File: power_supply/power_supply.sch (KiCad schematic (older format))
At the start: 51 parts, among them J1 Conn_01x04_Male, J2 Conn_01x03_Male, J3 Conn_01x03_Male, J4 Conn_01x03_Male, J5 Conn_01x02_Male, J6 Conn_01x02_Male, U1 LM7815_TO220, U2 LM7915_TO220, U3 LM7815_TO220

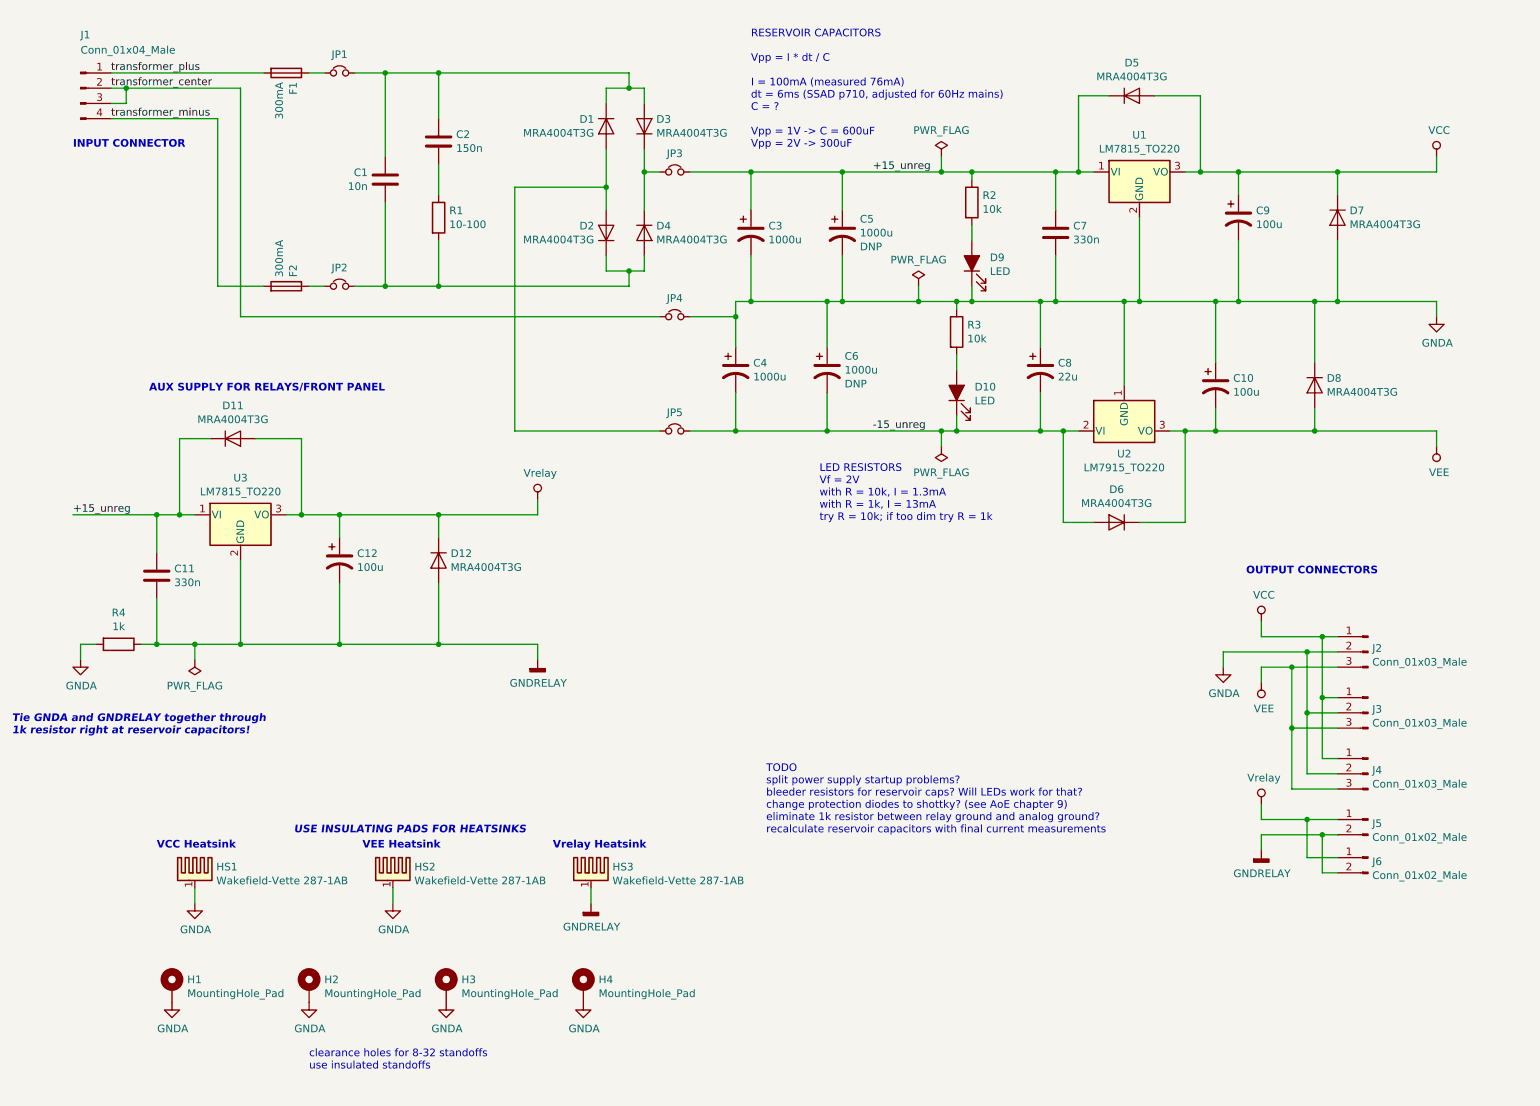
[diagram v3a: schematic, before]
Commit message: beautify schematic, update TODO, and tweak LEDs
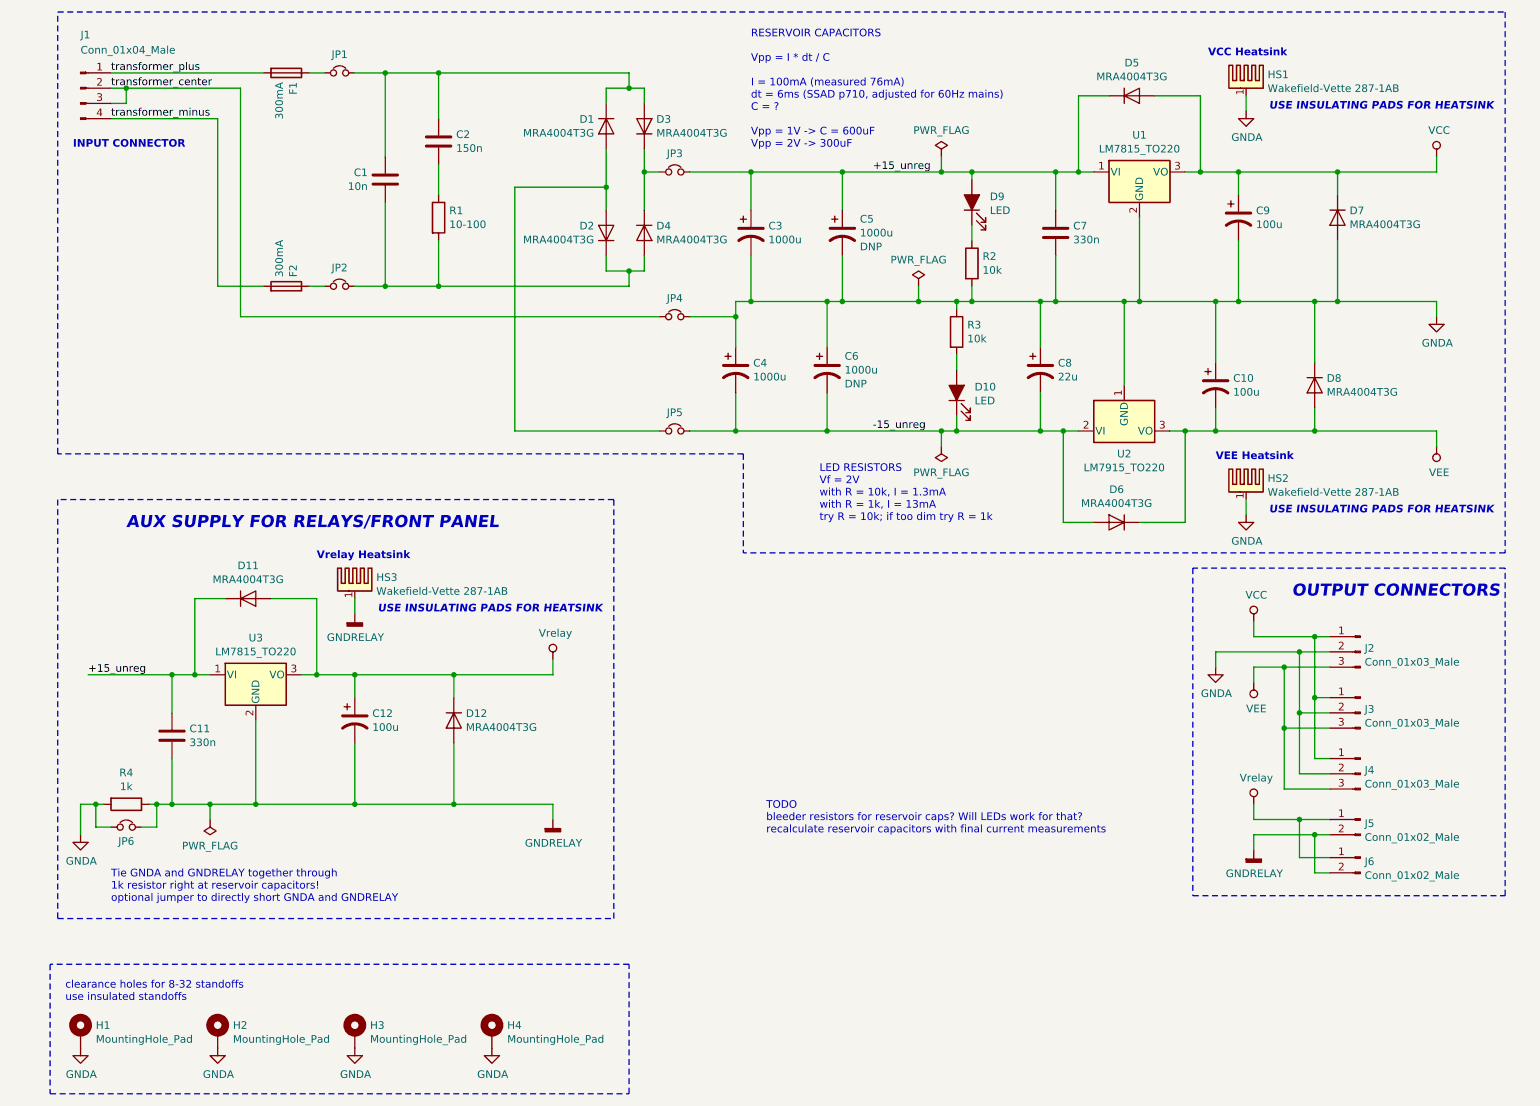
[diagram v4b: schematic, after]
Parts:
- added JP6: Jumper_NC_Small, Connector_PinHeader_2.54mm:PinHeader_1x02_P2.54mm_Vertical, symbol Device:Jumper_NC_Small
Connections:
- net +15_unreg: now also D9.2 (A); no longer R2.1
- net GNDA: now also R2.2, JP6.1; no longer D9.1 (K)
- net GNDRELAY: now also JP6.2
- new net: D9.1 (K), R2.1
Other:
- note added: "TODO\nbleeder resistors for reservoir caps? Will LEDs work for that?\nrecalculate reservoir capacitors with final current measurements"
- note added: "Tie GNDA and GNDRELAY together through\n1k resistor right at reservoir capacitors!\noptional jumper to directly short GNDA and GNDRELAY"
- note added: "USE INSULATING PADS FOR HEATSINK"
- note removed: "TODO\nsplit power supply startup problems?\nbleeder resistors for reservoir caps? Will LEDs work for that?\nchange protection diodes to shottky? (see AoE chapter 9)\neliminate 1k resistor between relay ground and analog ground?\nrecalculate reservoir capacitors with final current measurements"
- note removed: "Tie GNDA and GNDRELAY together through\n1k resistor right at reservoir capacitors!"
- note removed: "USE INSULATING PADS FOR HEATSINKS"
- moved on the sheet: C11, C12, D11, D12, D9, H1, H2, H3, H4, HS1, HS2, HS3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

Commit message: add OSHW/license to schematic
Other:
- note added: "CC-BY-SA 3.0"
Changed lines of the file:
@@
 	1    0    0    -1
 $EndComp
+$Comp
+L Graphic:Logo_Open_Hardware_Large #LOGO?
+U 1 1 5CFA7166
+P 5400 7400
+F 0 "#LOGO?" H 5400 7900 50  0001 C CNN
+F 1 "Logo_Open_Hardware_Large" H 5400 7000 50  0001 C CNN
+F 2 "" H 5400 7400 50  0001 C CNN
+F 3 "~" H 5400 7400 50  0001 C CNN
+	1    5400 7400
+	1    0    0    -1
+$EndComp
+Text Notes 5150 7900 0    50   ~ 10
+CC-BY-SA 3.0
 $EndSCHEMATC

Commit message: update text, and finalize damping resistor value
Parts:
- R1: value 10-100 -> 100
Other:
- note added: "RESERVOIR CAPACITORS\nC = I * dt / Vpp\n\nI = 250mA\ndt = 8.33ms\nVpp = 1-2V\n\nVpp = 1V -> C = 2000uF\nVpp = 2V -> C = 1000uF"
- note removed: "RESERVOIR CAPACITORS\n\nVpp = I * dt / C\n\nI = 100mA (measured 76mA)\ndt = 6ms (SSAD p710, adjusted for 60Hz mains)\nC = ?\n\nVpp = 1V -> C = 600uF\nVpp = 2V -> 300uF"
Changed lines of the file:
@@
 P 3350 2200
 F 0 "R1" H 3420 2246 50  0000 L CNN
-F 1 "10-100" H 3420 2155 50  0000 L CNN
+F 1 "100" H 3420 2155 50  0000 L CNN
 F 2 "Resistor_SMD:R_1206_3216Metric_Pad1.42x1.75mm_HandSolder" V 3280 2200 50  0001 C CNN
 F 3 "~" H 3350 2200 50  0001 C CNN
@@
 $EndComp
 Text Notes 5400 1750 0    50   ~ 0
-RESERVOIR CAPACITORS\n\nVpp = I * dt / C\n\nI = 100mA (measured 76mA)\ndt = 6ms (SSAD p710, adjusted for 60Hz mains)\nC = ?\n\nVpp = 1V -> C = 600uF\nVpp = 2V -> 300uF
+RESERVOIR CAPACITORS\nC = I * dt / Vpp\n\nI = 250mA\ndt = 8.33ms\nVpp = 1-2V\n\nVpp = 1V -> C = 2000uF\nVpp = 2V -> C = 1000uF
 Wire Wire Line
 	8250 4200 8250 3600

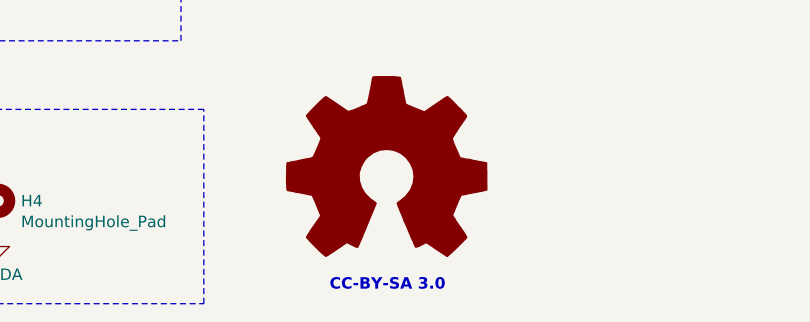
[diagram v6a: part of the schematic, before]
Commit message: change CC license version in schematic text from 3 to 4
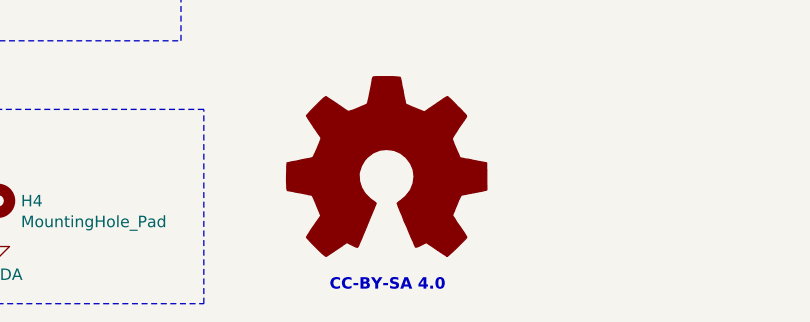
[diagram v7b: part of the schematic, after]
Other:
- note added: "CC-BY-SA 4.0"
- note removed: "CC-BY-SA 3.0"
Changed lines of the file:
@@
 	1    0    0    -1
 $EndComp
+Text Notes 5150 7900 0    50   ~ 10
+CC-BY-SA 4.0
 $Comp
-L Graphic:Logo_Open_Hardware_Large #LOGO?
+L Graphic:Logo_Open_Hardware_Large #LOGO1
 U 1 1 5CFA7166
 P 5400 7400
-F 0 "#LOGO?" H 5400 7900 50  0001 C CNN
+F 0 "#LOGO1" H 5400 7900 50  0001 C CNN
 F 1 "Logo_Open_Hardware_Large" H 5400 7000 50  0001 C CNN
 F 2 "" H 5400 7400 50  0001 C CNN
@@
 	1    0    0    -1
 $EndComp
-Text Notes 5150 7900 0    50   ~ 10
-CC-BY-SA 3.0
 $EndSCHEMATC

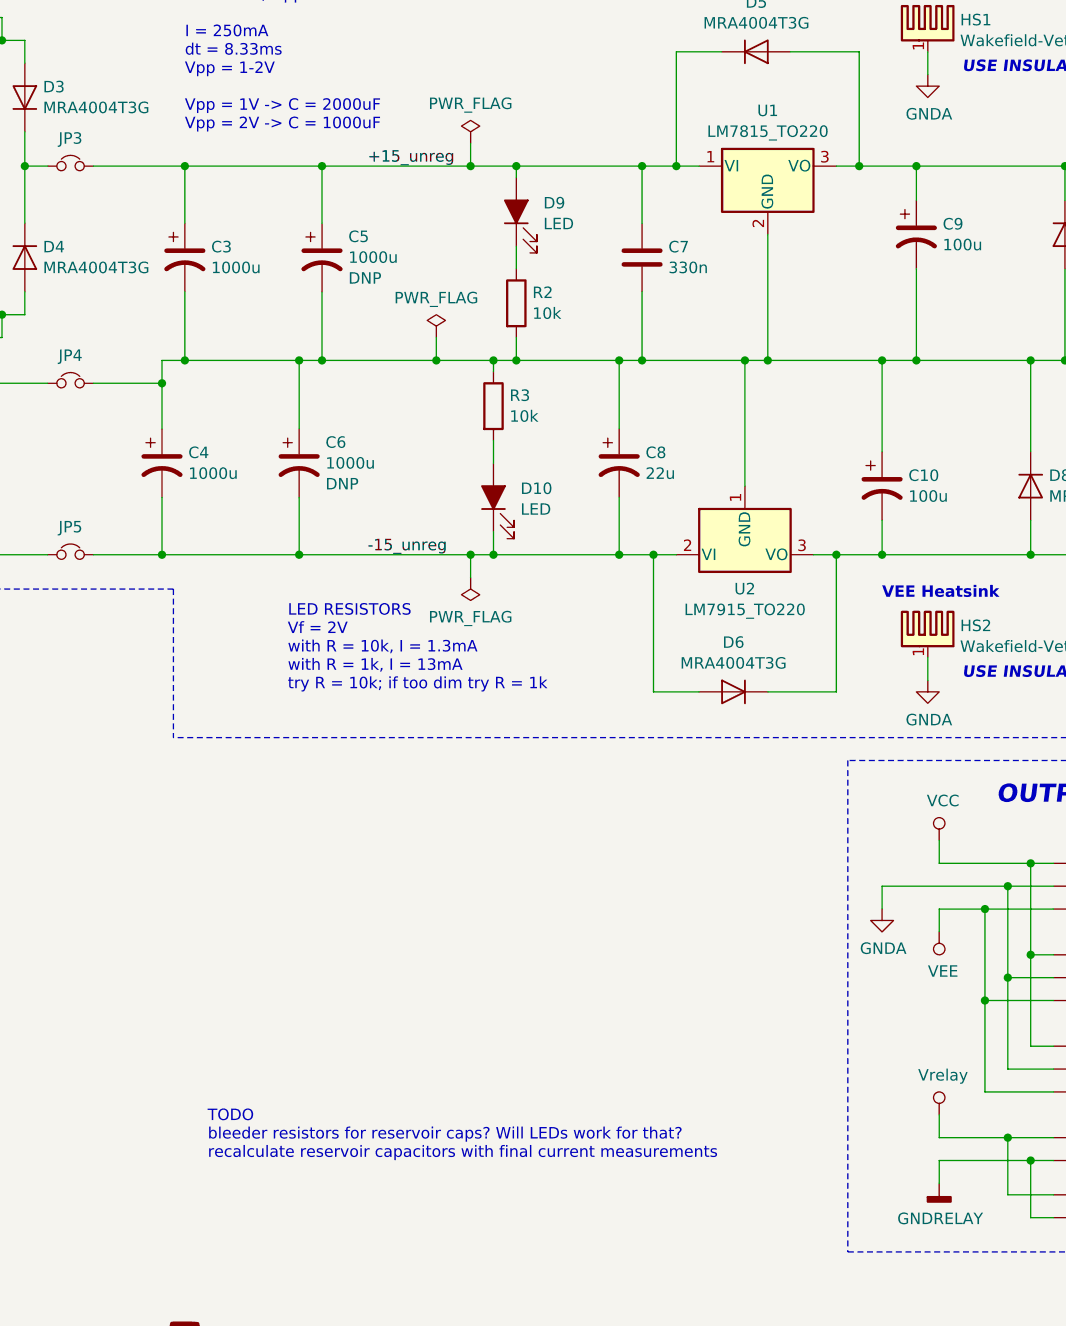
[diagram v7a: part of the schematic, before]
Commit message: remove second set of reservoir caps (deemed unnecessary for ripple and take up too much space)
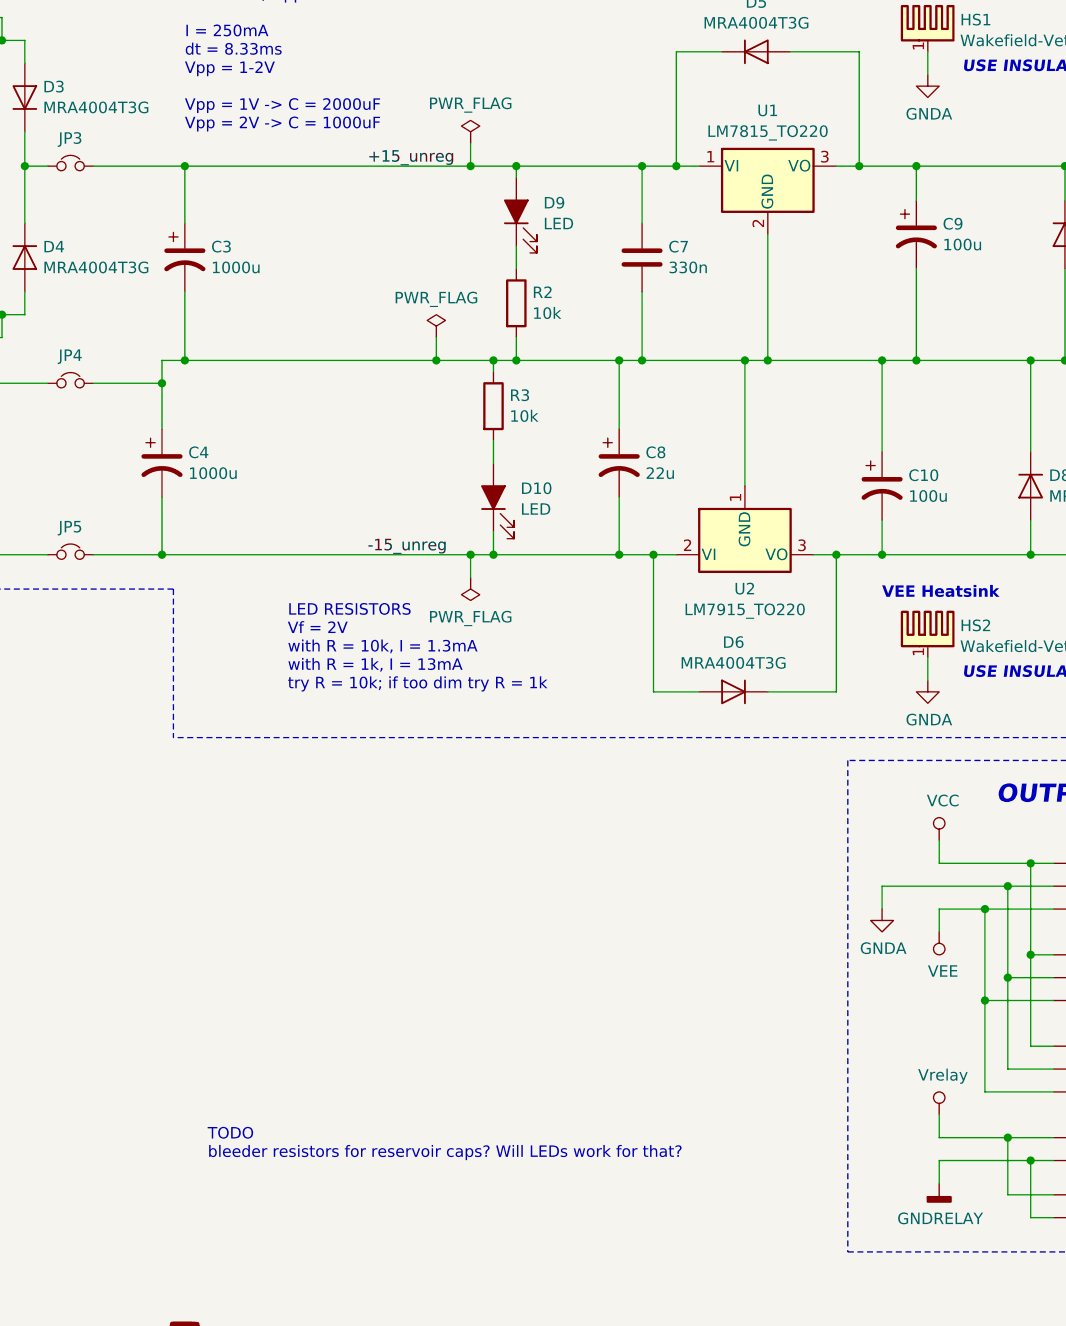
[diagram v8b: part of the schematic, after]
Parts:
- removed C5, C6: 1000u, Capacitor_THT:CP_Radial_D12.5mm_P5.00mm, symbol Device:CP1
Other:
- note added: "TODO\nbleeder resistors for reservoir caps? Will LEDs work for that?"
- note removed: "TODO\nbleeder resistors for reservoir caps? Will LEDs work for that?\nrecalculate reservoir capacitors with final current measurements"
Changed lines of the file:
@@
 $EndComp
 Text Notes 5500 6250 0    50   ~ 0
-TODO\nbleeder resistors for reservoir caps? Will LEDs work for that?\nrecalculate reservoir capacitors with final current measurements
+TODO\nbleeder resistors for reservoir caps? Will LEDs work for that?
 $Comp
 L Device:CP1 C8
@@
 	5400 2450 5400 2750
 Connection ~ 5400 1900
-Wire Wire Line
-	5400 1900 6000 1900
 Connection ~ 5300 3600
 Wire Wire Line
@@
 Wire Wire Line
 	5000 2850 5300 2850
-Connection ~ 5900 2750
-Wire Wire Line
-	5900 2750 6000 2750
-Wire Wire Line
-	5900 2750 5400 2750
-Wire Wire Line
-	5300 3600 5900 3600
-Wire Wire Line
-	5900 3350 5900 3600
-Wire Wire Line
-	5900 2750 5900 3050
-$Comp
-L Device:CP1 C6
-U 1 1 5CB06522
-P 5900 3200
-F 0 "C6" H 6015 3291 50  0000 L CNN
-F 1 "1000u" H 6015 3200 50  0000 L CNN
-F 2 "Capacitor_THT:CP_Radial_D12.5mm_P5.00mm" H 5900 3200 50  0001 C CNN
-F 3 "http://nichicon-us.com/english/products/pdfs/e-uvr.pdf" H 5900 3200 50  0001 C CNN
-F 4 "Nichicon" H 5900 3200 50  0001 C CNN "Manufacturer"
-F 5 "UVR1H102MHD" H 5900 3200 50  0001 C CNN "Manufacturer PN"
-F 6 "Digikey" H 5900 3200 50  0001 C CNN "Distributor"
-F 7 "493-1111-ND" H 5900 3200 50  0001 C CNN "Distributor PN"
-F 8 "https://www.digikey.com/product-detail/en/nichicon/UVR1H102MHD/493-1111-ND/588852" H 5900 3200 50  0001 C CNN "URL"
-F 9 "0.86" H 5900 3200 50  0001 C CNN "Unit Price"
-F 10 "DNP" H 6015 3109 50  0000 L CNN "DNP"
-	1    5900 3200
-	1    0    0    -1
-$EndComp
-Wire Wire Line
-	6000 2450 6000 2750
-Wire Wire Line
-	6000 2150 6000 1900
-$Comp
-L Device:CP1 C5
-U 1 1 5CB0609E
-P 6000 2300
-F 0 "C5" H 6115 2391 50  0000 L CNN
-F 1 "1000u" H 6115 2300 50  0000 L CNN
-F 2 "Capacitor_THT:CP_Radial_D12.5mm_P5.00mm" H 6000 2300 50  0001 C CNN
-F 3 "http://nichicon-us.com/english/products/pdfs/e-uvr.pdf" H 6000 2300 50  0001 C CNN
-F 4 "Nichicon" H 6000 2300 50  0001 C CNN "Manufacturer"
-F 5 "UVR1H102MHD" H 6000 2300 50  0001 C CNN "Manufacturer PN"
-F 6 "Digikey" H 6000 2300 50  0001 C CNN "Distributor"
-F 7 "493-1111-ND" H 6000 2300 50  0001 C CNN "Distributor PN"
-F 8 "https://www.digikey.com/product-detail/en/nichicon/UVR1H102MHD/493-1111-ND/588852" H 6000 2300 50  0001 C CNN "URL"
-F 9 "0.86" H 6000 2300 50  0001 C CNN "Unit Price"
-F 10 "DNP" H 6115 2209 50  0000 L CNN "DNP"
-	1    6000 2300
-	1    0    0    -1
-$EndComp
 Wire Wire Line
 	3850 2000 3850 3600
@@
 	6850 1900 7400 1900
 Connection ~ 6850 1900
-Wire Wire Line
-	6000 2750 6500 2750
-Connection ~ 6000 2750
-Wire Wire Line
-	6000 1900 6650 1900
-Connection ~ 6000 1900
-Wire Wire Line
-	5900 3600 6650 3600
-Connection ~ 5900 3600
 Wire Wire Line
 	5300 2850 5300 2750
@@
 	1    0    0    -1
 $EndComp
+Wire Wire Line
+	5400 1900 6650 1900
+Wire Wire Line
+	5300 3600 6650 3600
+Wire Wire Line
+	5400 2750 6500 2750
 $EndSCHEMATC
